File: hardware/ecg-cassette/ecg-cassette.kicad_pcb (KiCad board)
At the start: 2 copper layers, 80.4 x 50 mm, 4 parts, among them J2 02x07_Horizontal_Pin_Header, U1 MAX30003

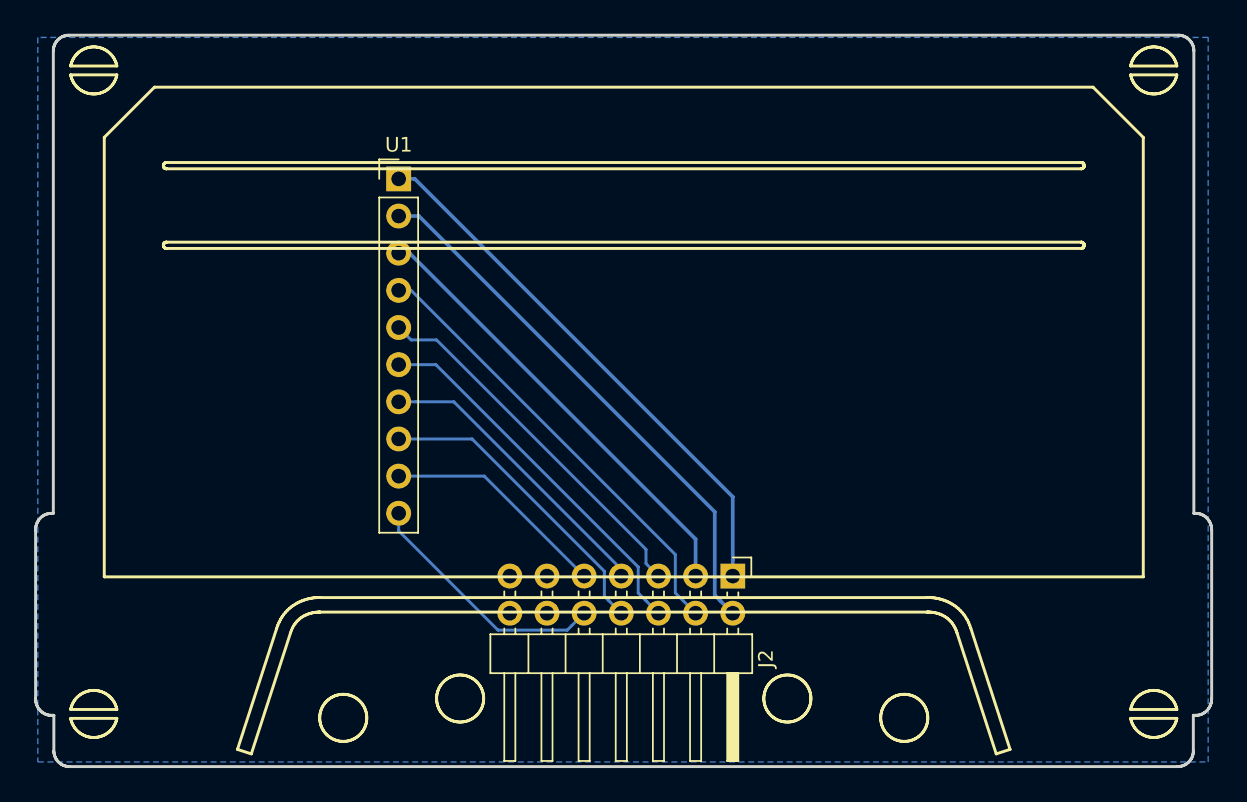
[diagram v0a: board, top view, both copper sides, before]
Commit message: [hw] Finish ecg module v0.2 design
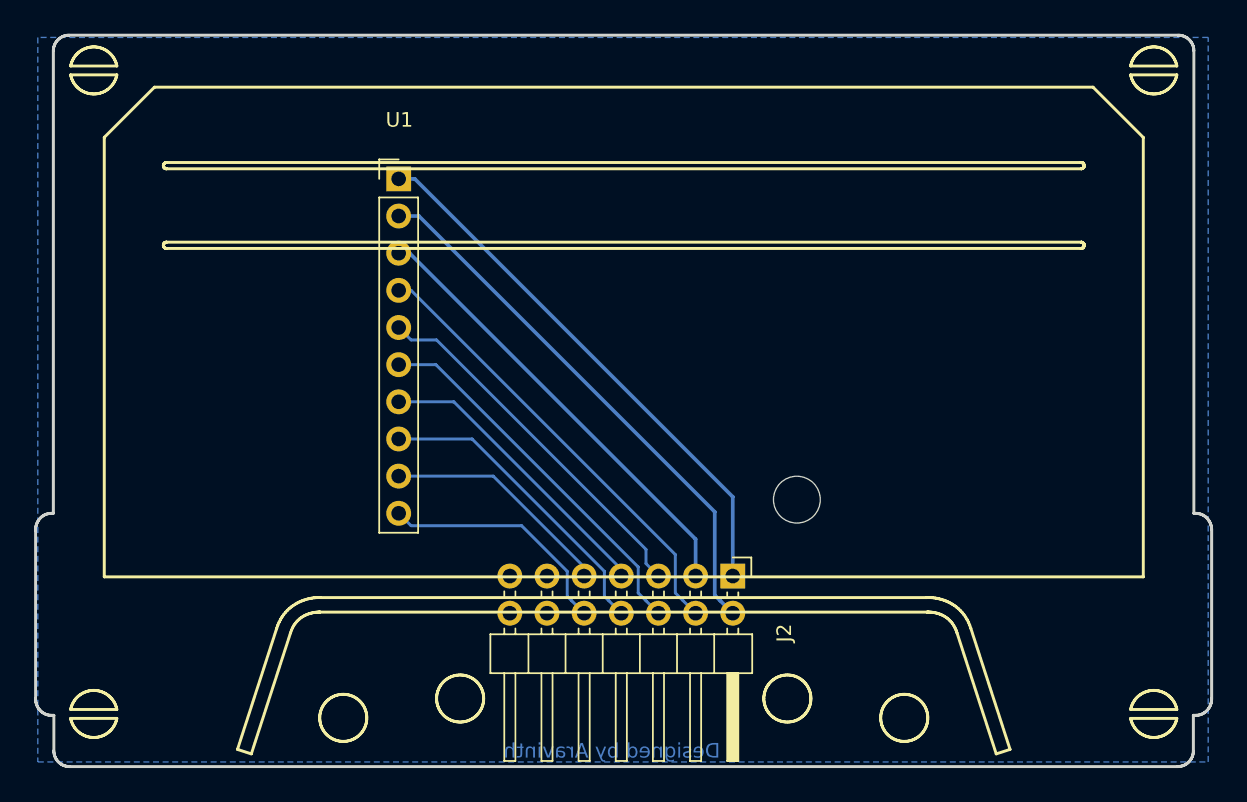
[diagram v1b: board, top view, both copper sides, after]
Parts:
- added G***: LOGO, ARABEAT:LOGO, B.Cu at (155.8, 120.8)
- added REF**: M3, MountingHole:MountingHole_3.2mm_M3, F.Cu at (152.2, 131.9)
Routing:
- net /MISO: track 17.2 -> 16.5 mm
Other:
- board text added: "Designed by Aravinth"

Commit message: [hw] Update libraries of ECG Cassette
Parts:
- G***: footprint ARABEAT:LOGO -> ECG-CASSETTE:LOGO
- REF**: footprint ARABEAT:CASSETTE-MARK -> ECG-CASSETTE:CASSETTE-MARK
- REF**: footprint ARABEAT:CASSETTE-SILKSCREEN -> ECG-CASSETTE:CASSETTE-SILKSCREEN

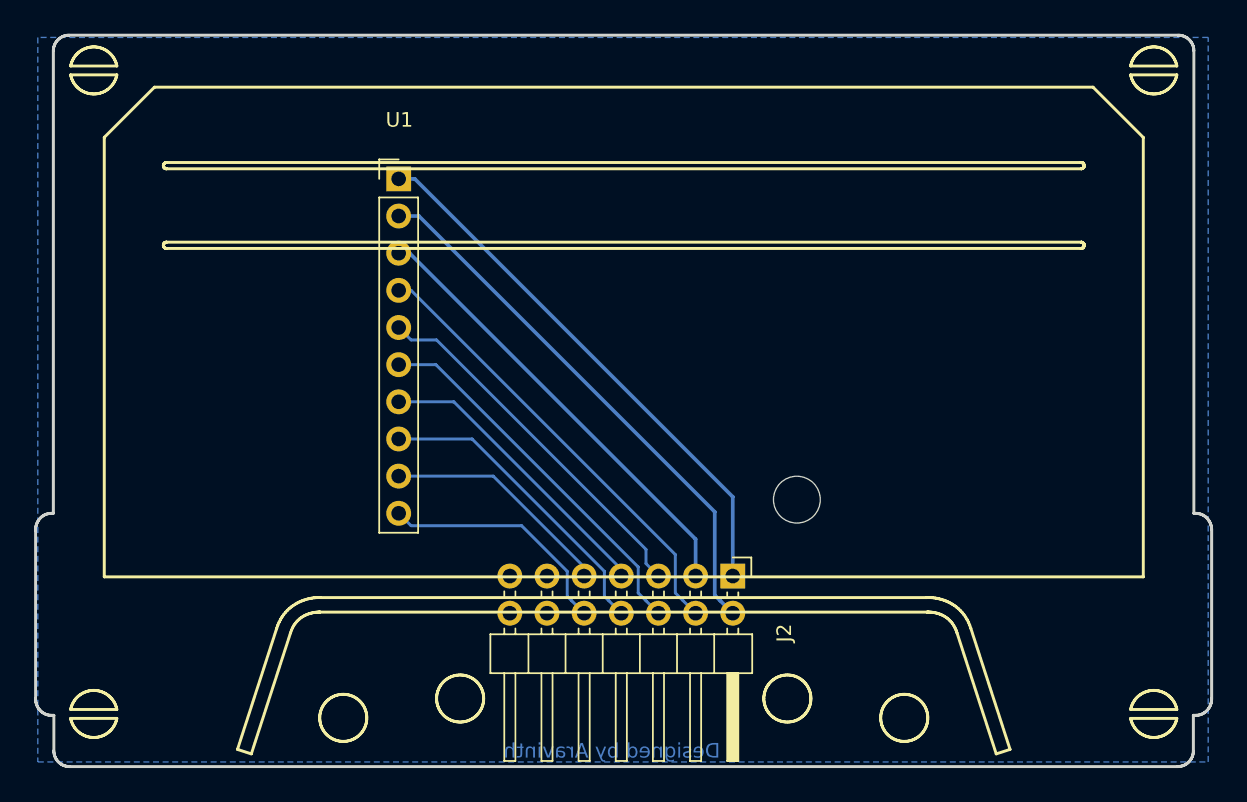
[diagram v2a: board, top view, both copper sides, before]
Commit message: [hw] Update ECG Cassette with new footprints & schematics
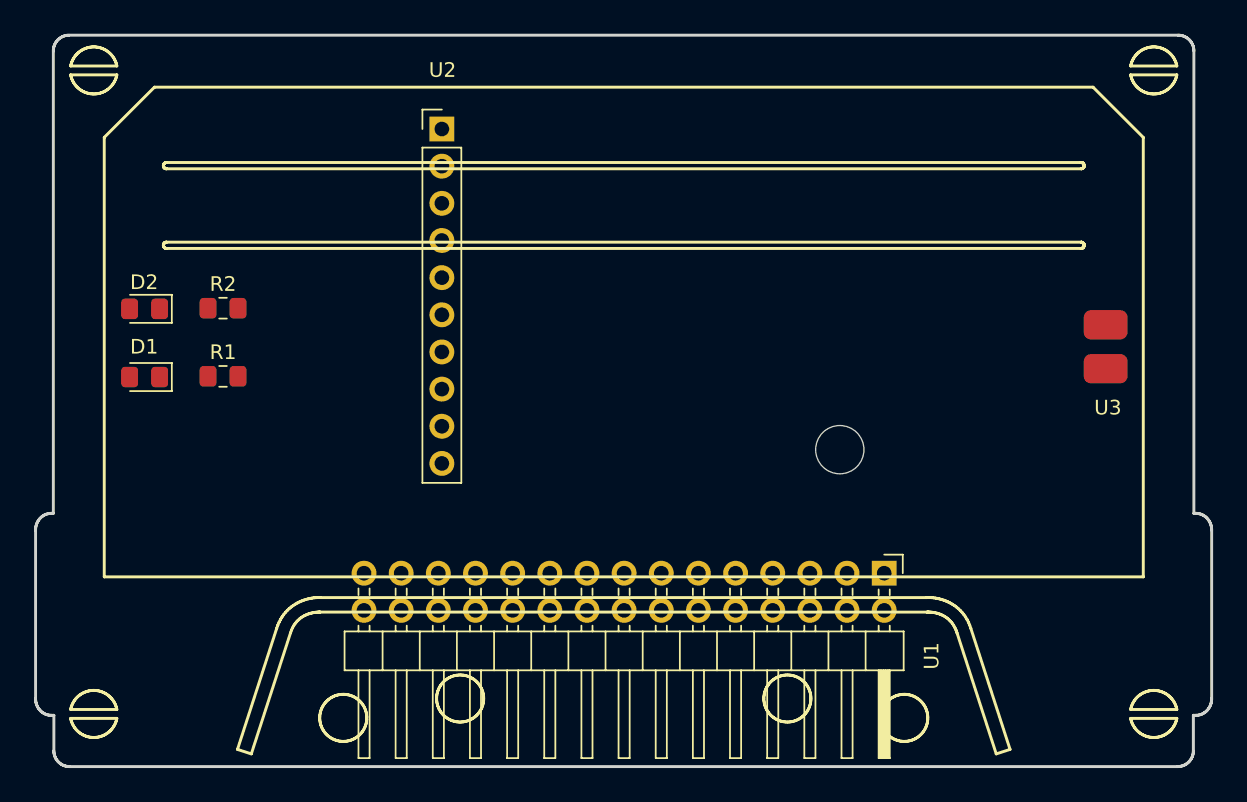
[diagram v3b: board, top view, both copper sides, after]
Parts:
- removed G***: LOGO, ECG-CASSETTE:LOGO
- removed J2: 02x07_Horizontal_Pin_Header, Connector_PinHeader_2.54mm:PinHeader_2x07_P2.54mm_Horizontal
- removed REF**: CASSETTE-MARK, ECG-CASSETTE:CASSETTE-MARK
- removed REF**: CASSETTE-SILKSCREEN, ECG-CASSETTE:CASSETTE-SILKSCREEN
- removed REF**: M3, MountingHole:MountingHole_3.2mm_M3
- added D1: RED_STATUS_LED, LED_SMD:LED_0805_2012Metric_Pad1.15x1.40mm_HandSolder, F.Cu at (107.6, 123.5)
- added D2: GREEN_PWR_LED, LED_SMD:LED_0805_2012Metric_Pad1.15x1.40mm_HandSolder, F.Cu at (107.6, 118.9)
- added LOGO: LOGO, ARABEAT:ECG-CASSETTE-LOGO, B.Cu at (140.4, 125.2)
- added MARK: CASSETTE-MARK, ARABEAT:MCU-CASSETTE-MARK, F.Cu at (100.0, 100.0)
- added R1: 1K, Resistor_SMD:R_0805_2012Metric_Pad1.15x1.40mm_HandSolder, F.Cu at (113.0, 123.5)
- added R2: 1K, Resistor_SMD:R_0805_2012Metric_Pad1.15x1.40mm_HandSolder, F.Cu at (113.0, 118.8)
- added SILK: CASSETTE-SILKSCREEN, ARABEAT:ECG-CASSETTE-SILKSCREEN-EDGECUT, F.Cu at (100.0, 100.0)
- added U2: MAX30003, PROTOCENTRAL:MAX30003, F.Cu at (128.0, 106.6)
- added U3: ECG-WIRE-TO-BOARD, ARABEAT:ECG-WIRE-TO-BOARD, F.Cu at (173.3, 120.0)
- U1: value MAX30003 -> 02x15_PIN_HEADER_SOCKET; footprint PROTOCENTRAL:MAX30003 -> Connector_PinHeader_2.54mm:PinHeader_2x15_P2.54mm_Horizontal
- moved U1 42.8 mm to (158.2, 137.0), turned to 270 degrees
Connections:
- U1 pad 1: /GND -> 5V
- U1 pad 10: /MISO -> (no net)
- U1 pad 2: /VCC -> (no net)
- U1 pad 3: /GND -> (no net)
- U1 pad 4: /INT2 -> D2
- U1 pad 5: /INT1 -> D3
- U1 pad 6: /FCLK -> (no net)
- U1 pad 7: /CSB -> (no net)
- U1 pad 8: /SCK -> (no net)
- U1 pad 9: /MOSI -> D7
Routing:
- net /GND: track 68.2 -> 0.00 mm
- net /VCC: track 37.4 -> 0.00 mm
- net /INT2: track 31.0 -> 0.00 mm
- net /FCLK: track 25.8 -> 0.00 mm
- net /INT1: track 25.4 -> 0.00 mm
- net /SCK: track 21.2 -> 0.00 mm
- net /CSB: track 20.4 -> 0.00 mm
- net /MISO: track 16.5 -> 0.00 mm
- net /MOSI: track 15.9 -> 0.00 mm
- removed copper zone on B.Cu, net /GND
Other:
- net class PWR removed
- net class SIG removed
- rule pad_to_mask_clearance: 0.051 -> 0
- rule trace_min: 0.1524 -> 0.2
- rule via_min_size: 0.6 -> 0.4
- board text removed: "Designed by Aravinth"

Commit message: [hw] Make ECG Module production ready
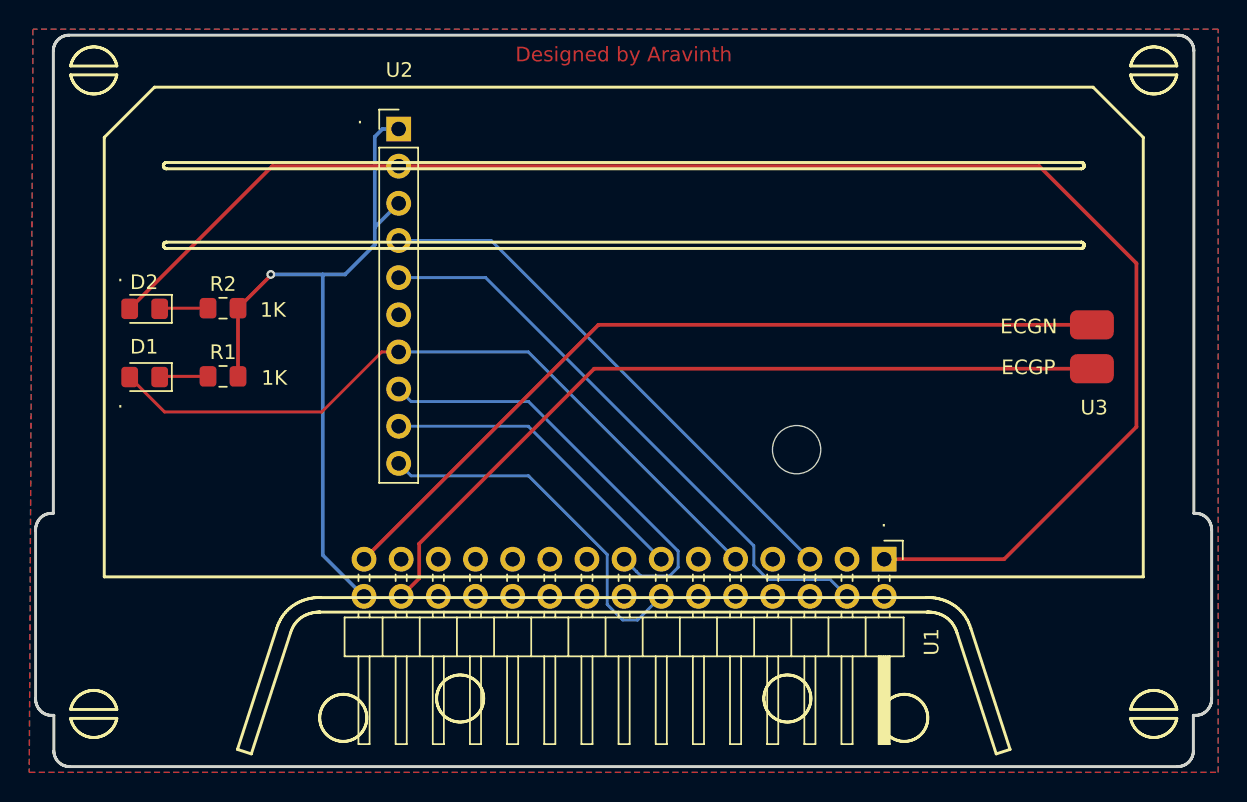
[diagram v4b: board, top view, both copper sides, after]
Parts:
- removed LOGO: LOGO, ARABEAT:ECG-CASSETTE-LOGO
- added G***: LOGO, ARABEAT:CASSETTE-LOGO, B.Cu at (154.6, 121.1)
- moved U2 2.95 mm to (125.0, 106.6)
- moved U1 0.96 mm to (158.2, 136.0)
- moved U3 0.94 mm to (172.4, 120.0)
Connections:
- U1 pad 10: (no net) -> Net-(U1-Pad10)
- U1 pad 11: (no net) -> Net-(U1-Pad11)
- U1 pad 12: (no net) -> Net-(U1-Pad12)
- U1 pad 16: (no net) -> Net-(U1-Pad16)
- U1 pad 17: (no net) -> Net-(U1-Pad17)
- U1 pad 18: (no net) -> Net-(U1-Pad18)
- U1 pad 19: (no net) -> Net-(U1-Pad19)
- U1 pad 2: (no net) -> Net-(U1-Pad2)
- U1 pad 20: (no net) -> Net-(U1-Pad20)
- U1 pad 21: (no net) -> Net-(U1-Pad21)
- U1 pad 22: (no net) -> Net-(U1-Pad22)
- U1 pad 23: (no net) -> Net-(U1-Pad23)
- U1 pad 24: (no net) -> Net-(U1-Pad24)
- U1 pad 25: (no net) -> Net-(U1-Pad25)
- U1 pad 26: (no net) -> Net-(U1-Pad26)
- U1 pad 27: (no net) -> Net-(U1-Pad27)
- U1 pad 3: (no net) -> Net-(U1-Pad3)
- U1 pad 6: (no net) -> Net-(U1-Pad6)
- U1 pad 7: (no net) -> Net-(U1-Pad7)
- U1 pad 8: (no net) -> Net-(U1-Pad8)
- U2 pad 6: (no net) -> Net-(U2-Pad6)
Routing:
- net 5V: track 0.00 -> 107.8 mm
- net ECGN: track 0.00 -> 56.4 mm
- net ECGP: track 0.00 -> 55.1 mm
- net GND: track 0.00 -> 50.6 mm, vias 0 -> 1
- net D7: track 0.00 -> 50.0 mm
- net D2: track 0.00 -> 40.5 mm
- net D3: track 0.00 -> 37.1 mm
- net D13: track 0.00 -> 29.2 mm
- net D12: track 0.00 -> 25.1 mm
- net D11: track 0.00 -> 21.7 mm
- net Net-(D2-Pad1): track 0.00 -> 3.33 mm
- net Net-(D1-Pad1): track 0.00 -> 3.33 mm
- added copper zone on F.Cu, net 5V
- added copper zone on B.Cu, net GND
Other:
- net class PWR added: clearance 0.254, trace_width 0.254, via_dia 0.6, via_drill 0.3
- net class SIGNAL added: clearance 0.2032, trace_width 0.2032, via_dia 0.6, via_drill 0.3
- rule trace_min: 0.2 -> 0.1524
- rule via_min_size: 0.4 -> 0.6
- board text added: "."
- board text added: "Designed by Aravinth"
- board text added: "ECG Module v0.2 : Designed by Aravinth"
- board text added: "ECGN"
- board text added: "ECGP"
- board text added: "www.arabeat.aravinth.info"
